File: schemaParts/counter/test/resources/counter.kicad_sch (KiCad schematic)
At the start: 5 parts, among them U1 74LS393

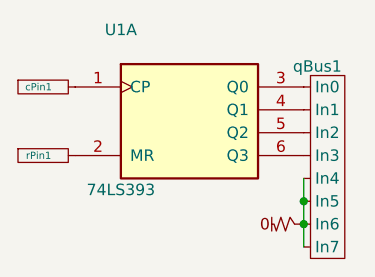
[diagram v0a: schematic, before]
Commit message: Actualise unit test for dCounter
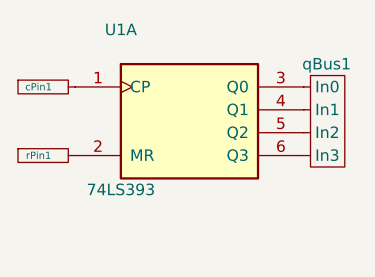
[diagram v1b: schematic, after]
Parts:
- removed pulldown1: pull_down, symbol chip:PULLDOWN
- removed qBus1: InBus, symbol Tests:InBus
- added qBus1: InBus4x, symbol Tests:InBus4x
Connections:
- net at U1.3 (Q0): now also qBus1.0 (In0)
- net at U1.4 (Q1): now also qBus1.1 (In1)
- net at U1.5 (Q2): now also qBus1.2 (In2)
- net at U1.6 (Q3): now also qBus1.3 (In3)
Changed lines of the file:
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@@
 (kicad_sch (version 20230121) (generator eeschema)
   (paper "A4")
-  (junction (at 132.08 81.28) (diameter 0) (color 0 0 0 0)
-  )
-  (junction (at 132.08 83.82) (diameter 0) (color 0 0 0 0)
-  )
-  (wire (pts (xy 132.08 81.28) (xy 132.08 83.82))
-    (stroke (width 0) (type default))
-  )
-  (wire (pts (xy 132.08 83.82) (xy 132.08 86.36))
-    (stroke (width 0) (type default))
-  )
-  (wire (pts (xy 132.08 78.74) (xy 132.08 81.28))
-    (stroke (width 0) (type default))
-  )
-  (symbol (lib_id "chip:PULLDOWN") (at 132.08 83.82 0) (unit 1)
-    (in_bom yes) (on_board yes) (dnp no)
-    (property "Reference" "pulldown1" (at 128.524 88.9 0)
-      (effects (font (size 1.27 1.27)) hide)
-    )
-    (property "Value" "pull_down" (at 128.524 88.9 0)
-      (effects (font (size 1.27 1.27)) hide)
-    )
-    (property "Footprint" "" (at 128.524 86.36 0)
-      (effects (font (size 1.27 1.27)) hide)
-    )
-    (property "Datasheet" "" (at 128.524 86.36 0)
-      (effects (font (size 1.27 1.27)) hide)
-    )
-    (pin "1")
-    (instances
-      (project "counter"
-        (path "/dca00733-6e59-4b89-b3a6-bb50926963b6"
-          (reference "pulldown1") (unit 1)
-        )
-      )
-    )
-  )
   (symbol (lib_id "Tests:OutPin") (at 106.68 76.2 0) (unit 1)
     (in_bom yes) (on_board yes) (dnp no)
@@
         (path "/dca00733-6e59-4b89-b3a6-bb50926963b6"
           (reference "rPin1") (unit 1)
+        )
+      )
+    )
+  )
+  (symbol (lib_id "Tests:InBus4x") (at 132.08 72.39 0) (unit 1)
+    (in_bom yes) (on_board yes) (dnp no)
+    (property "Reference" "qBus1" (at 134.62 66.04 0)
+      (effects (font (size 1.27 1.27)))
+    )
+    (property "Value" "InBus4x" (at 123.178 66.802 0)
+      (effects (font (size 1.27 1.27)) hide)
+    )
+    (property "Footprint" "" (at 132.83 77.47 0)
+      (effects (font (size 1.27 1.27)) hide)
+    )
+    (property "Datasheet" "" (at 132.83 77.47 0)
+      (effects (font (size 1.27 1.27)) hide)
+    )
+    (pin "2")
+    (pin "0")
+    (pin "3")
+    (pin "1")
+    (instances
+      (project "counter"
+        (path "/dca00733-6e59-4b89-b3a6-bb50926963b6"
+          (reference "qBus1") (unit 1)
         )
       )
@@
         )
       )
-    )
-  )
-  (symbol (lib_id "Tests:InBus") (at 132.08 77.47 0) (unit 1)
-    (in_bom yes) (on_board yes) (dnp no)
-    (property "Reference" "qBus1" (at 133.592 66.294 0)
-      (effects (font (size 1.27 1.27)))
-    )
-    (property "Value" "InBus" (at 123.178 66.802 0)
-      (effects (font (size 1.27 1.27)) hide)
-    )
-    (property "Footprint" "" (at 132.83 77.47 0)
-      (effects (font (size 1.27 1.27)) hide)
-    )
-    (property "Datasheet" "" (at 132.83 77.47 0)
-      (effects (font (size 1.27 1.27)) hide)
-    )
-    (pin "4")
-    (pin "5")
-    (pin "6")
-    (pin "1")
-    (pin "7")
-    (pin "3")
-    (pin "2")
-    (pin "0")
-    (instances
-      (project "counter"
-        (path "/dca00733-6e59-4b89-b3a6-bb50926963b6"
-          (reference "qBus1") (unit 1)
-        )
-      )
